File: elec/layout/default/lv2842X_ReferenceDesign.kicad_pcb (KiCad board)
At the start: 2 copper layers, 8 parts, among them U3 10µH ±20%

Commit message: Fix ato reference names
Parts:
- R1: value 7.5kΩ ±1% 62.5mW -> 8.2kΩ ±1% 62.5mW
- R2: value 22kΩ ±1% 62.5mW -> 10kΩ ±1% 62.5mW
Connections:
- net hv-1 renamed VIN

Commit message: add better test coverage
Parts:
- added C3: 10µF ±10% 25V X5R, atopile:C0805-3b2e55, F.Cu at (50.0, -5.00)
- added R1: 3.6kΩ ±1% 62.5mW, atopile:R0402-56259e, F.Cu at (60.0, -5.00)
- added R2: 20kΩ ±1% 62.5mW, atopile:R0402-56259e, F.Cu at (80.0, -5.00)
- added U2: , lib:SOT-23-6_L2.9-W1.6-P0.95-LS2.8-BR, F.Cu at (70.0, -5.00)
- C2, C3: value 100nF ±10% 50V X7R -> 10µF ±10% 25V X5R
- R1: value 8.2kΩ ±1% 62.5mW -> 4.7kΩ ±1% 62.5mW
- moved U1 41.1 mm to (40.0, -5.00)
- moved C2 30.1 mm to (30.0, -5.00)
- moved C1 22.0 mm to (20.0, -5.00), turned to 0 degrees
- moved U3 15.9 mm to (10.0, -5.00), turned to 0 degrees
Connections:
- C2 pad 1: VIN -> hv-1
- C3 pad 1: hv -> (no net)
- C3 pad 2: gnd -> gnd-1
- R1 pad 2: gnd -> gnd-1
- R2 pad 1: hv -> (no net)
- U2 pad 1: CB -> (no net)
- U2 pad 2: gnd-1 -> (no net)
- U2 pad 4: VIN -> (no net)
- U2 pad 5: VIN -> (no net)
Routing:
- net (no net): track 0.00 -> 5.07 mm, vias 0 -> 2
- net gnd: track 4.28 -> 0.00 mm, vias 2 -> 0
- net CB: track 2.36 -> 0.00 mm
- net gnd-1: track 2.70 -> 4.28 mm
- added copper zone on F.Cu, net (none)
- removed copper zone on F.Cu, net VIN
- removed copper zone on F.Cu, net hv

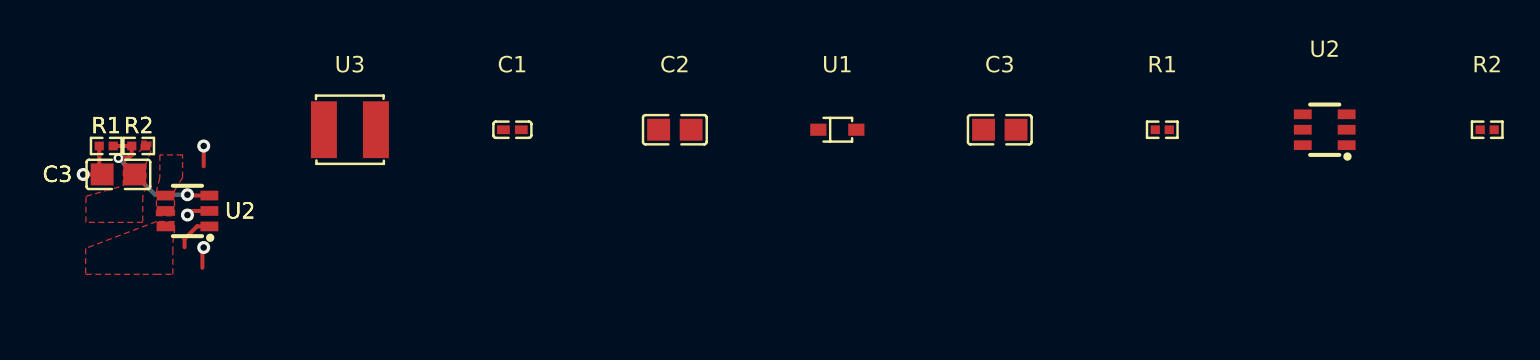
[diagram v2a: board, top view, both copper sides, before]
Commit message: Update layouts to kicad 9, add default build for layout reuse
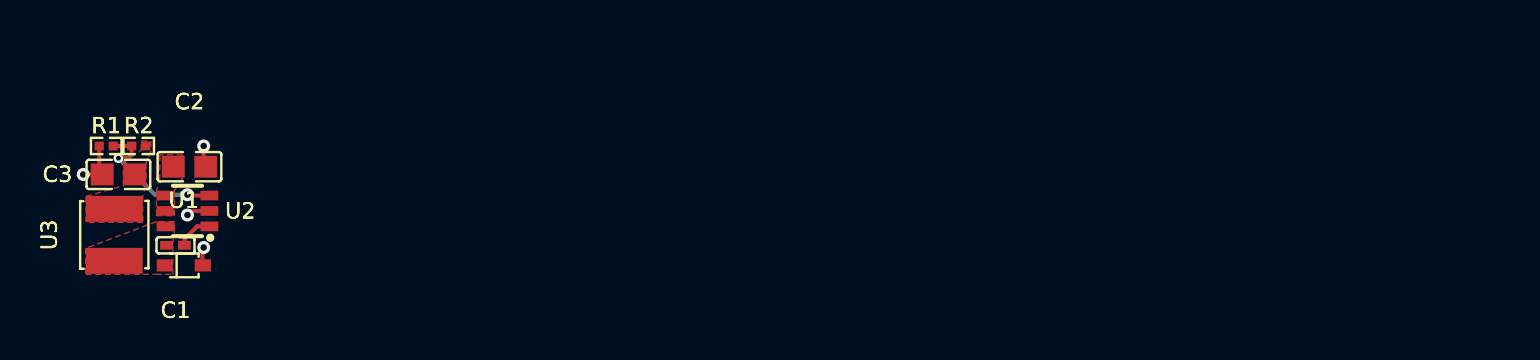
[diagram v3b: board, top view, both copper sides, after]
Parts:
- removed the C3 at (50.0, -5.00)
- removed the R1 at (60.0, -5.00)
- removed the R2 at (80.0, -5.00)
- removed the U2 at (70.0, -5.00)
- C2: value 10µF ±10% 25V X5R -> 4.7µF ±10% 25V X5R
- R1: value 4.7kΩ ±1% 62.5mW -> 10kΩ ±1% 62.5mW
- moved U1 41.1 mm to (-0.23, 3.35)
- moved C2 30.0 mm to (0.12, -2.73)
- moved C1 21.9 mm to (-0.74, 2.11), turned to 180 degrees
- moved U3 15.9 mm to (-4.50, 1.47), turned to 90 degrees
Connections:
- net line renamed FB
- C2 pad 1: hv-1 -> SHDN_hash
- C2 pad 2: gnd-1 -> gnd
- C3 pad 1: (no net) -> hv
- R2 pad 1: (no net) -> hv
- U1 pad 2: gnd -> gnd-1
- U2 pad 1: (no net) -> CB
- U2 pad 2: (no net) -> gnd
- U2 pad 4: (no net) -> SHDN_hash
- U2 pad 5: (no net) -> SHDN_hash
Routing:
- net (no net): track 5.07 -> 0.00 mm, vias 2 -> 0
- net gnd: track 0.00 -> 2.70 mm, vias 0 -> 2
- net CB: track 0.00 -> 2.36 mm
- removed copper zone on F.Cu, net SW
